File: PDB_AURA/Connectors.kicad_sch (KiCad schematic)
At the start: 29 parts, among them J300 XT30PW-F, J301 XT30PW-F, J302 532617012, J303 XT30PW-F, J304 XT30PW-F, Q300 HSK10N06, Q301 HSK10N06, U300 LTV-217-B-G, U301 LTV-217-B-G, U302 INA219AIDCNR

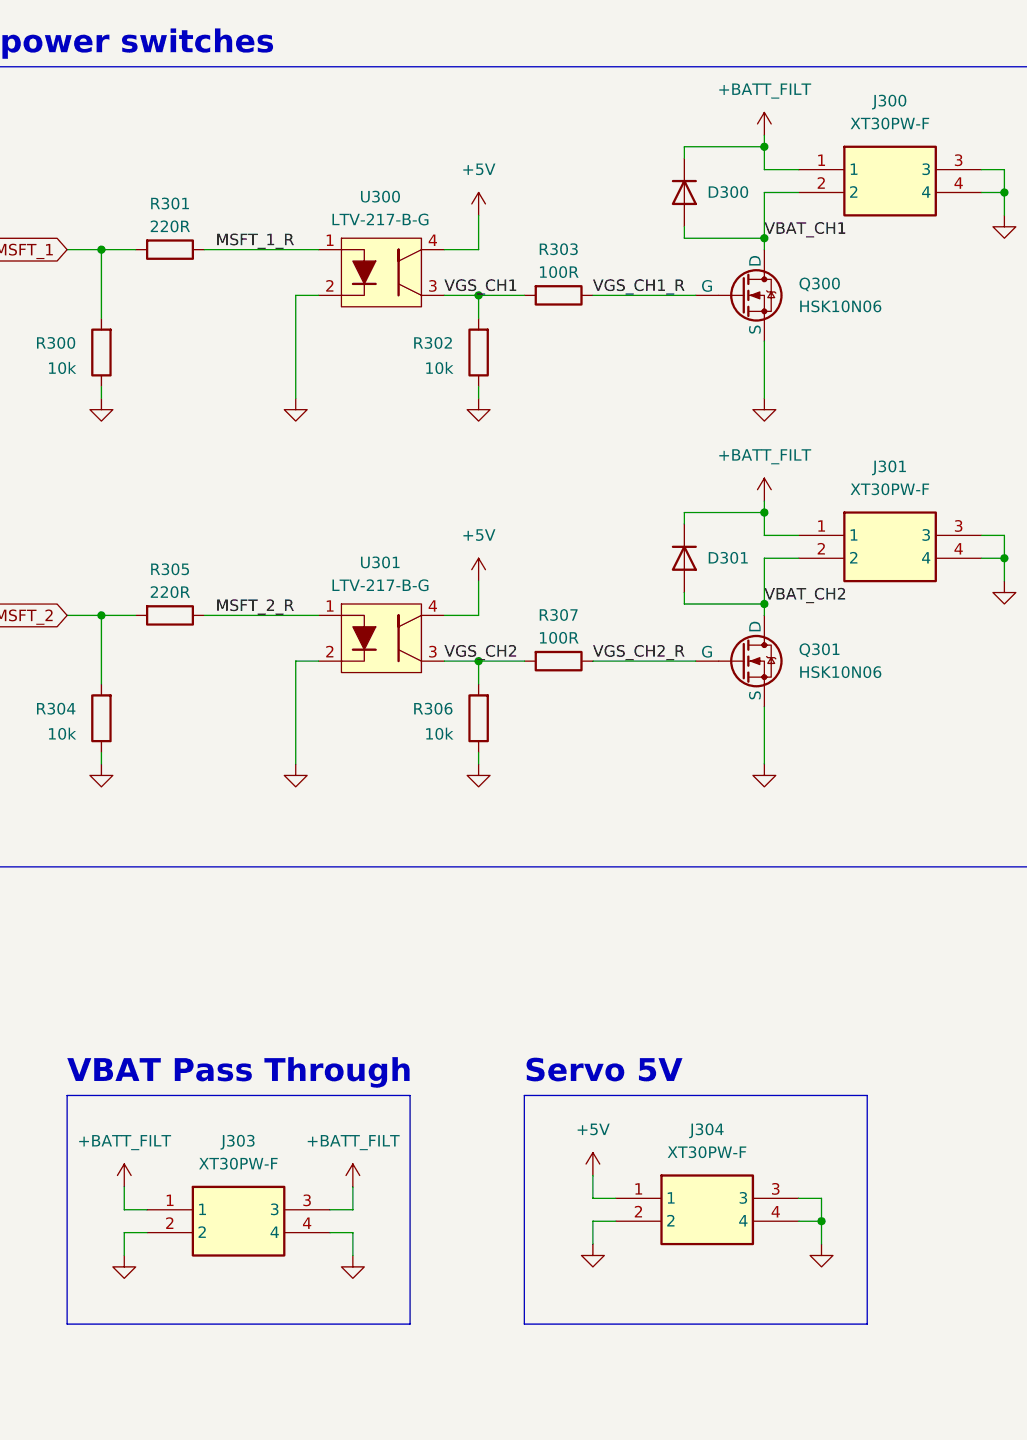
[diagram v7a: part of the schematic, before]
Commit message: Re Routing some of the power board
Connectors had positive and negative the wrong way around, and some of the routing did not look good.
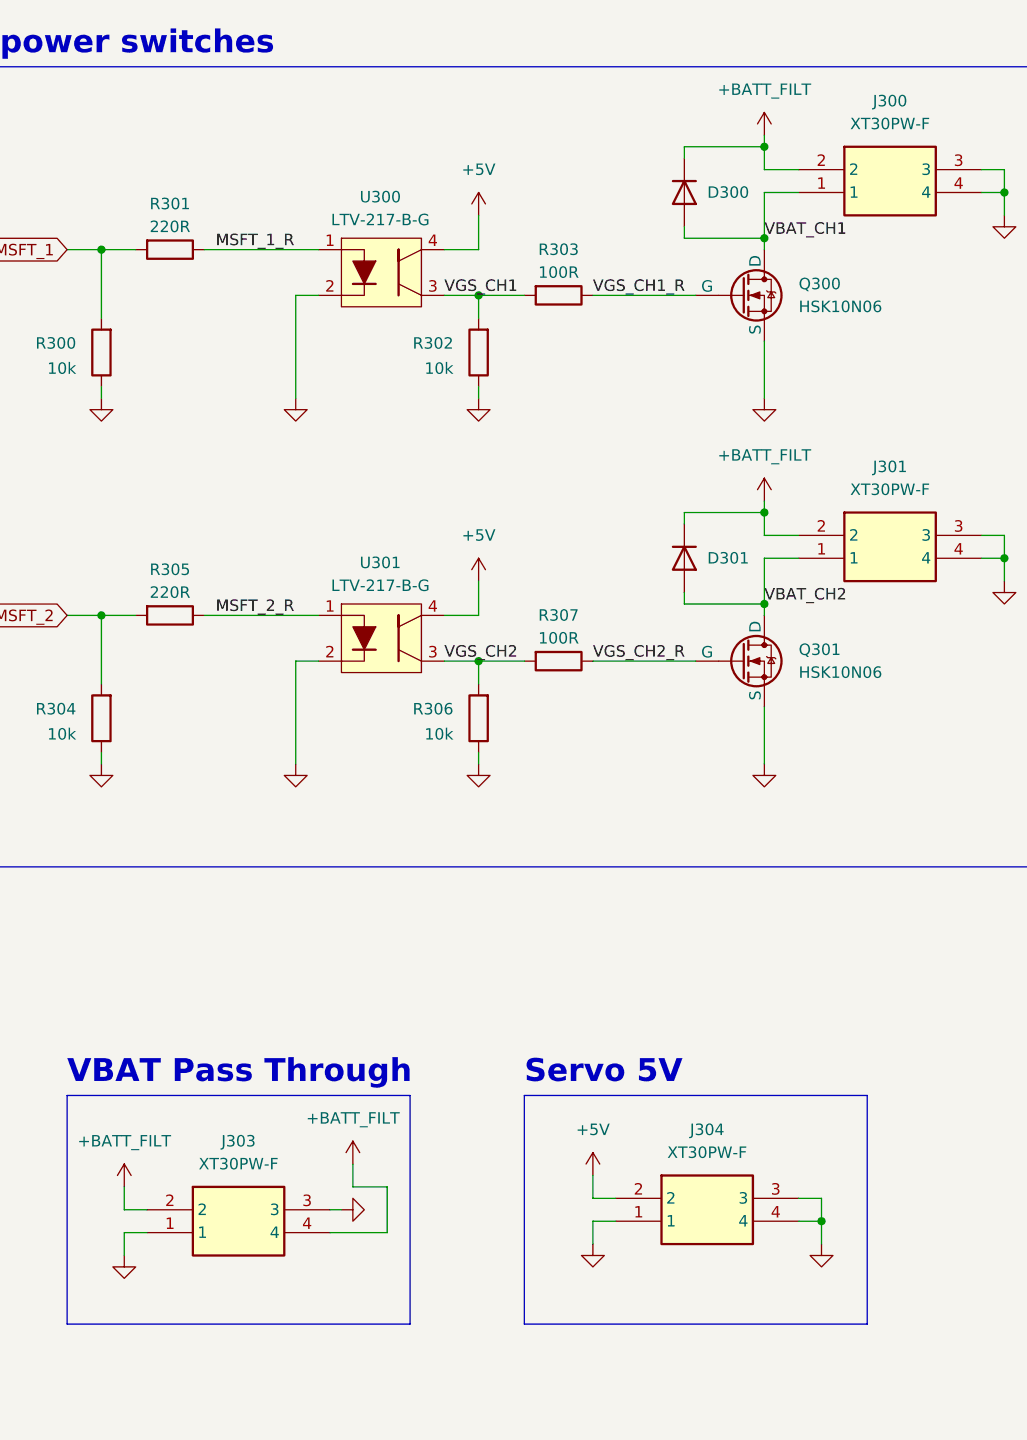
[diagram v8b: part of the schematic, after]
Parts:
- J300, J301, J303, J304: footprint XT30PWF:XT30PWF -> XT30PWF
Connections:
- net +5V: now also J304.2; no longer J304.1
- net +BATT_FILT: now also J300.2, J301.2, J303.2, J303.4; no longer J300.1, J301.1, J303.1, J303.3
- net GND: now also J303.1, J303.3, J304.1; no longer J303.2, J303.4, J304.2
- net VBAT_CH1: now also J300.1; no longer J300.2
- net VBAT_CH2: now also J301.1; no longer J301.2
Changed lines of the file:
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@@
 	(wire
 		(pts
+			(xy 73.66 167.64) (xy 67.31 167.64)
+		)
+		(stroke
+			(width 0)
+			(type default)
+		)
+	)
+	(wire
+		(pts
 			(xy 252.73 63.5) (xy 252.73 66.04)
 		)
@@
 	(wire
 		(pts
-			(xy 170.18 82.55) (xy 182.88 82.55)
+			(xy 69.85 160.02) (xy 69.85 162.56)
 		)
 		(stroke
@@
 	(wire
 		(pts
-			(xy 121.92 163.83) (xy 119.38 163.83)
+			(xy 170.18 82.55) (xy 182.88 82.55)
 		)
 		(stroke
@@
 	(wire
 		(pts
-			(xy 238.76 91.44) (xy 242.57 91.44)
+			(xy 121.92 163.83) (xy 119.38 163.83)
 		)
 		(stroke
@@
 	(wire
 		(pts
-			(xy 115.57 57.15) (xy 115.57 58.42)
+			(xy 238.76 91.44) (xy 242.57 91.44)
 		)
 		(stroke
@@
 	(wire
 		(pts
-			(xy 69.85 165.1) (xy 69.85 162.56)
+			(xy 115.57 57.15) (xy 115.57 58.42)
 		)
 		(stroke
@@
 	(wire
 		(pts
+			(xy 73.66 162.56) (xy 73.66 167.64)
+		)
+		(stroke
+			(width 0)
+			(type default)
+		)
+	)
+	(wire
+		(pts
 			(xy 229.87 140.97) (xy 229.87 139.7)
 		)
@@
 	(wire
 		(pts
-			(xy 67.31 165.1) (xy 69.85 165.1)
-		)
-		(stroke
-			(width 0)
-			(type default)
-		)
-	)
-	(wire
-		(pts
 			(xy 106.68 55.88) (xy 106.68 57.15)
 		)
@@
 	(wire
 		(pts
-			(xy 69.85 170.18) (xy 69.85 167.64)
+			(xy 68.58 165.1) (xy 67.31 165.1)
 		)
 		(stroke
@@
 	(wire
 		(pts
+			(xy 69.85 162.56) (xy 73.66 162.56)
+		)
+		(stroke
+			(width 0)
+			(type default)
+		)
+	)
+	(wire
+		(pts
 			(xy 142.24 52.07) (xy 139.7 52.07)
 		)
@@
 		)
 	)
-	(wire
-		(pts
-			(xy 67.31 167.64) (xy 69.85 167.64)
-		)
-		(stroke
-			(width 0)
-			(type default)
-		)
-	)
 	(label "VGS_CH1"
 		(at 80.01 63.5 0)
@@
 			)
 		)
-		(property "Footprint" "XT30PWF:XT30PWF"
+		(property "Footprint" "XT30PWF"
 			(at 135.89 185.09 0)
 			(effects
@@
 			)
 		)
-		(property "Footprint" "XT30PWF:XT30PWF"
+		(property "Footprint" "XT30PWF"
 			(at 135.89 144.45 0)
 			(effects
@@
 			)
 		)
-		(property "Footprint" "XT30PWF:XT30PWF"
+		(property "Footprint" "XT30PWF"
 			(at 115.57 258.75 0)
 			(effects
@@
 			)
 		)
-		(property "Footprint" "XT30PWF:XT30PWF"
+		(property "Footprint" "XT30PWF"
 			(at 63.5 260.02 0)
 			(effects
@@
 	(symbol
 		(lib_id "power:+BATT")
-		(at 69.85 162.56 0)
+		(at 69.85 160.02 0)
 		(unit 1)
 		(exclude_from_sim no)
@@
 		(fields_autoplaced yes)
 		(property "Reference" "#PWR032"
-			(at 69.85 166.37 0)
+			(at 69.85 163.83 0)
 			(effects
 				(font
@@
 		)
 		(property "Value" "+BATT_FILT"
-			(at 69.85 157.48 0)
+			(at 69.85 154.94 0)
 			(effects
 				(font
@@
 		)
 		(property "Footprint" ""
-			(at 69.85 162.56 0)
+			(at 69.85 160.02 0)
 			(effects
 				(font
@@
 		)
 		(property "Datasheet" ""
-			(at 69.85 162.56 0)
+			(at 69.85 160.02 0)
 			(effects
 				(font
@@
 		)
 		(property "Description" "Power symbol creates a global label with name \"+BATT\""
-			(at 69.85 162.56 0)
+			(at 69.85 160.02 0)
 			(effects
 				(font
@@
 	(symbol
 		(lib_id "power:GND")
-		(at 69.85 170.18 0)
+		(at 68.58 165.1 90)
 		(unit 1)
 		(exclude_from_sim no)
@@
 		(fields_autoplaced yes)
 		(property "Reference" "#PWR04"
-			(at 69.85 176.53 0)
+			(at 74.93 165.1 0)
 			(effects
 				(font
@@
 		)
 		(property "Value" "GND"
-			(at 69.85 175.26 0)
+			(at 73.66 165.1 0)
 			(effects
 				(font
@@
 		)
 		(property "Footprint" ""
-			(at 69.85 170.18 0)
+			(at 68.58 165.1 0)
 			(effects
 				(font
@@
 		)
 		(property "Datasheet" ""
-			(at 69.85 170.18 0)
+			(at 68.58 165.1 0)
 			(effects
 				(font
@@
 		)
 		(property "Description" "Power symbol creates a global label with name \"GND\" , ground"
-			(at 69.85 170.18 0)
+			(at 68.58 165.1 0)
 			(effects
 				(font
